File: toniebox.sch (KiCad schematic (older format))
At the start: 129 parts, among them K2 Micro_SD_Card_Det_Hirose_DM3CS, K4 Conn_01x03, K9 Conn_01x03, T11 FDV301N, T360 FDV301N, T4 FDV301N, T5 FDV301N, T6 FDV301N, T7 FDV301N, U1 TLV320DAC3100, U2 CC3200R1M2RGCR, U3 IS25LQ032B-JNLE, U4 MMA8451QT, U8 AP2112K-3.3, U9 AP2120N-1.8

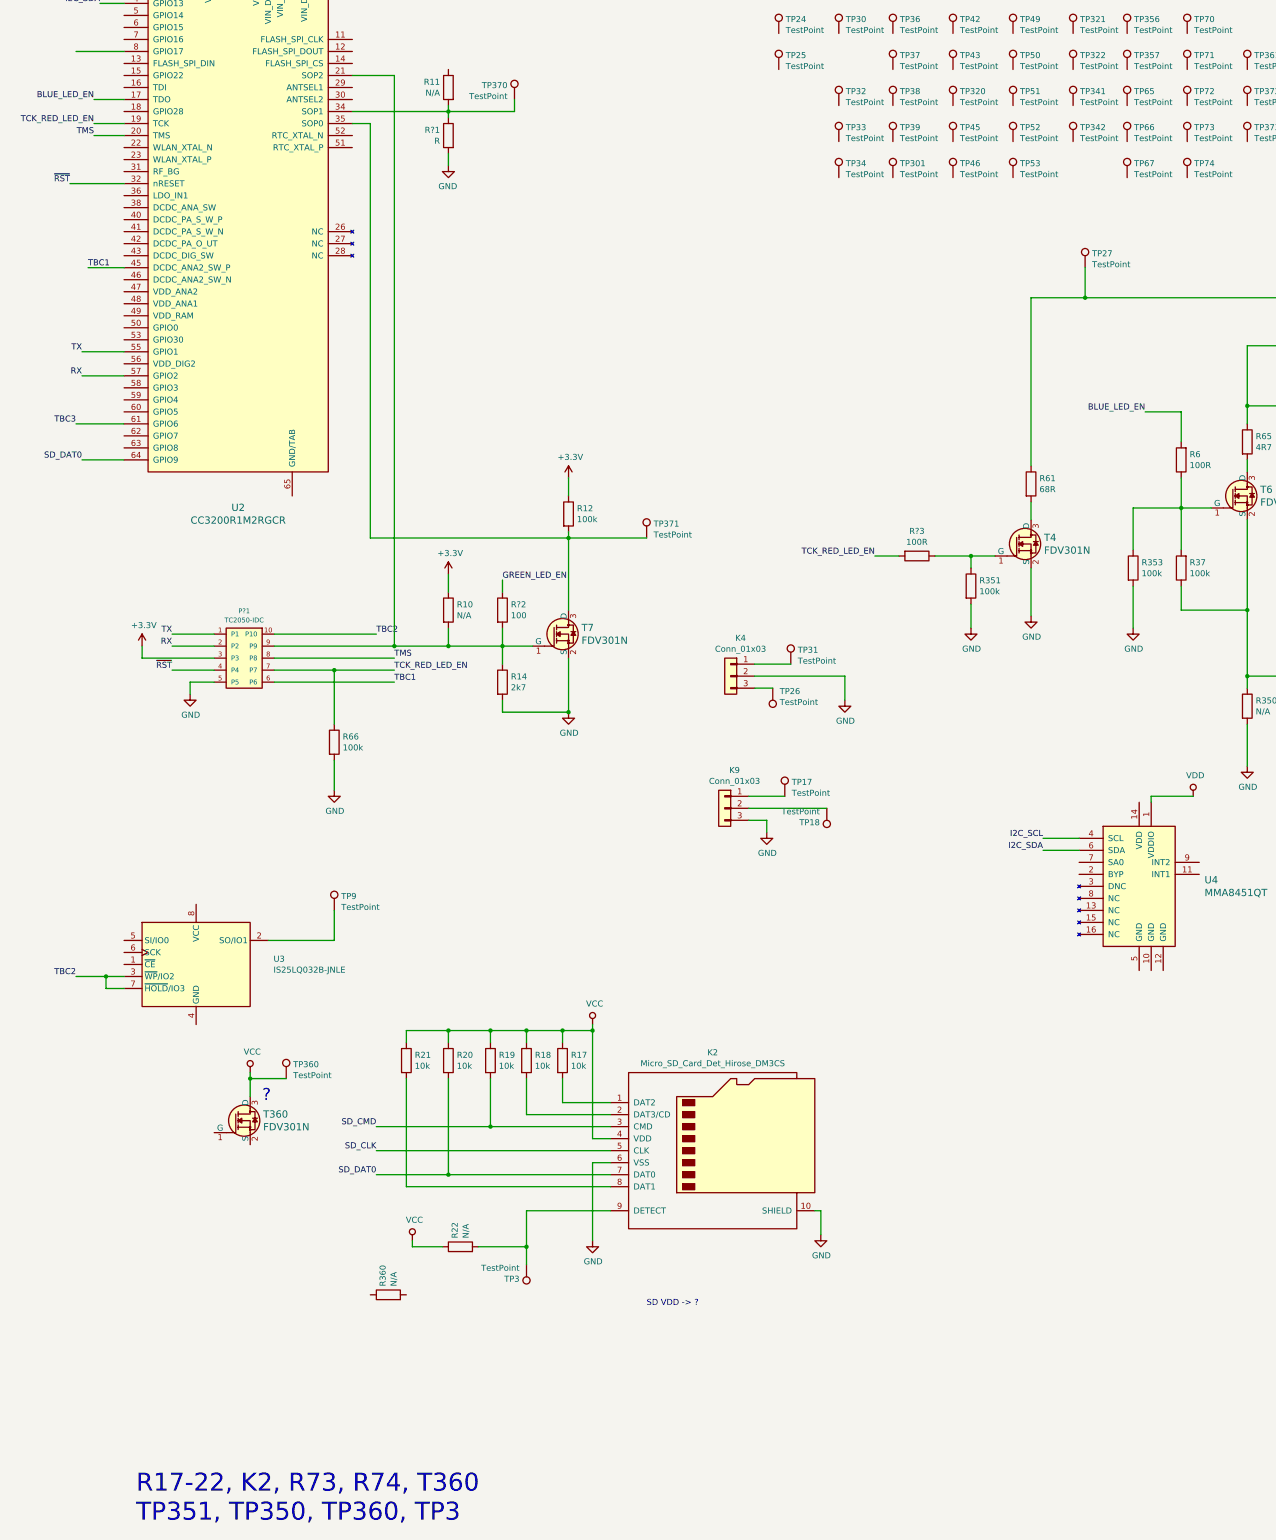
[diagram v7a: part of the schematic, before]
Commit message: battery, ear connectors;datasheets
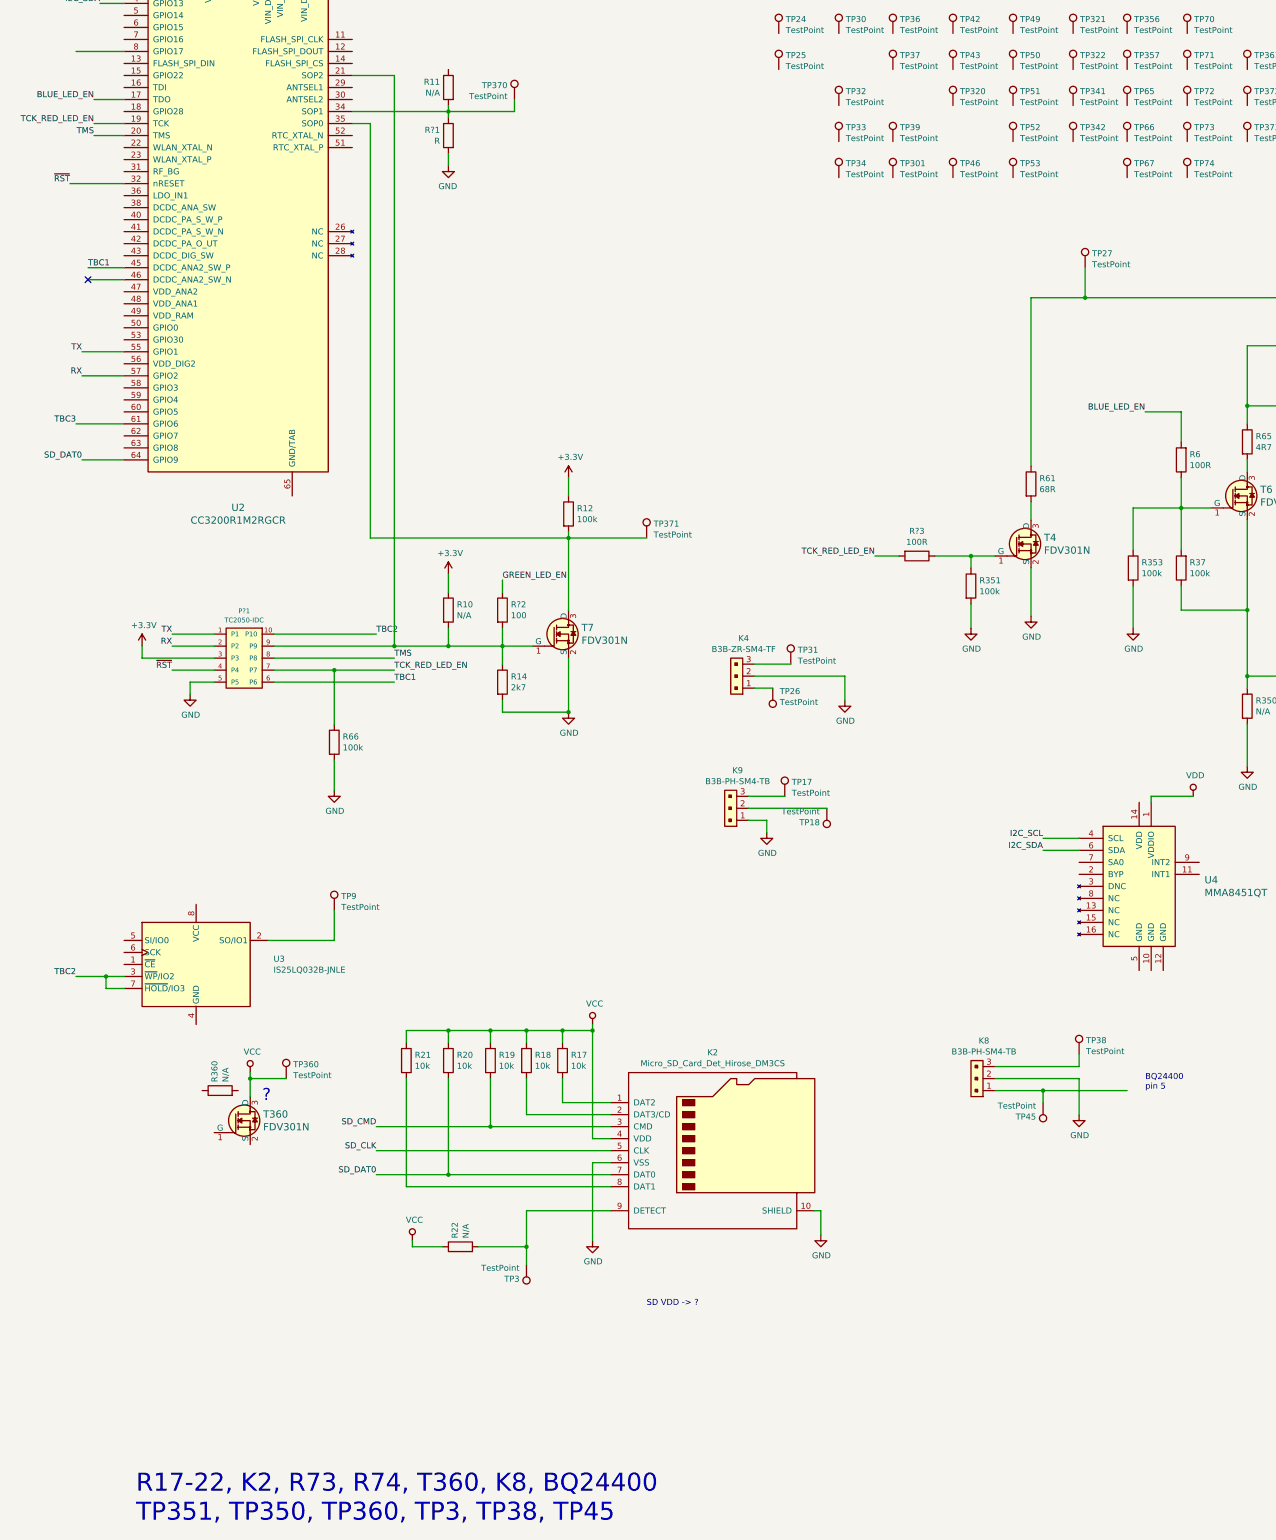
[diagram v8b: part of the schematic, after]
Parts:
- removed K4, K9: Conn_01x03, symbol Connector_Generic:Conn_01x03
- added K4: B3B-ZR-SM4-TF, symbol dk_Rectangular-Connectors-Headers-Male-Pins:B3B-PH-K-S_LF__SN_
- added K8, K9: B3B-PH-SM4-TB, symbol dk_Rectangular-Connectors-Headers-Male-Pins:B3B-PH-K-S_LF__SN_
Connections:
- net GND: now also K4.2, K8.2, K9.1
- net at TP17.1: now also K9.3
- net at TP18.1: now also K9.2
- net at TP31.1: now also K4.3
- net at TP26.1: now also K4.1
- net at TP38.1: now also K8.3
- net at TP45.1: now also K8.1
- no-connect marks 0 -> 1
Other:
- note added: "BQ24400\npin 5\n"
- note added: "R17-22, K2, R73, R74, T360, K8, BQ24400\nTP351, TP350, TP360, TP3, TP38, TP45"
- note removed: "R17-22, K2, R73, R74, T360\nTP351, TP350, TP360, TP3"
- moved on the sheet: R360, TP38, TP45
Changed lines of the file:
@@
 L Connector:TestPoint TP38
 U 1 1 5E31677D
-P 7450 2800
-F 0 "TP38" H 7508 2918 50  0000 L CNN
-F 1 "TestPoint" H 7508 2827 50  0000 L CNN
-F 2 "" H 7650 2800 50  0001 C CNN
-F 3 "~" H 7650 2800 50  0001 C CNN
-	1    7450 2800
+P 9000 10700
+F 0 "TP38" H 9058 10818 50  0000 L CNN
+F 1 "TestPoint" H 9058 10727 50  0000 L CNN
+F 2 "" H 9200 10700 50  0001 C CNN
+F 3 "~" H 9200 10700 50  0001 C CNN
+	1    9000 10700
 	1    0    0    -1
 $EndComp
@@
 L Connector:TestPoint TP45
 U 1 1 5E3167E1
-P 7950 3100
-F 0 "TP45" H 8008 3218 50  0000 L CNN
-F 1 "TestPoint" H 8008 3127 50  0000 L CNN
-F 2 "" H 8150 3100 50  0001 C CNN
-F 3 "~" H 8150 3100 50  0001 C CNN
-	1    7950 3100
-	1    0    0    -1
+P 8700 11100
+F 0 "TP45" H 8758 11218 50  0000 L CNN
+F 1 "TestPoint" H 8758 11127 50  0000 L CNN
+F 2 "" H 8900 11100 50  0001 C CNN
+F 3 "~" H 8900 11100 50  0001 C CNN
+	1    8700 11100
+	-1   0    0    1
 $EndComp
 $Comp
@@
 Wire Wire Line
 	6250 8650 6900 8650
-$Comp
-L Connector_Generic:Conn_01x03 K9
-U 1 1 5E37BC23
-P 6050 8650
-F 0 "K9" H 5968 8967 50  0000 C CNN
-F 1 "Conn_01x03" H 5968 8876 50  0000 C CNN
-F 2 "" H 6050 8650 50  0001 C CNN
-F 3 "~" H 6050 8650 50  0001 C CNN
-	1    6050 8650
-	-1   0    0    -1
-$EndComp
 Wire Wire Line
 	6300 7450 6600 7450
@@
 Wire Wire Line
 	6300 7550 7050 7550
-$Comp
-L Connector_Generic:Conn_01x03 K4
-U 1 1 5E34806A
-P 6100 7550
-F 0 "K4" H 6018 7867 50  0000 C CNN
-F 1 "Conn_01x03" H 6018 7776 50  0000 C CNN
-F 2 "" H 6100 7550 50  0001 C CNN
-F 3 "~" H 6100 7550 50  0001 C CNN
-	1    6100 7550
-	-1   0    0    -1
-$EndComp
 $Comp
 L Connector:TestPoint TP18
@@
 	4400 12450 4400 12300
 Text Notes 1150 14600 0    150  ~ 0
-R17-22, K2, R73, R74, T360\nTP351, TP350, TP360, TP3
+R17-22, K2, R73, R74, T360, K8, BQ24400\nTP351, TP350, TP360, TP3, TP38, TP45
 Text Notes 5400 12800 0    50   ~ 0
 SD VDD -> ?
@@
 L Device:R R360
 U 1 1 5E72EE90
-P 3250 12700
-F 0 "R360" H 3320 12746 50  0000 L CNN
-F 1 "N/A" H 3320 12655 50  0000 L CNN
-F 2 "" V 3180 12700 50  0001 C CNN
-F 3 "~" H 3250 12700 50  0001 C CNN
-	1    3250 12700
+P 1850 11000
+F 0 "R360" H 1920 11046 50  0000 L CNN
+F 1 "N/A" H 1920 10955 50  0000 L CNN
+F 2 "" V 1780 11000 50  0001 C CNN
+F 3 "~" H 1850 11000 50  0001 C CNN
+	1    1850 11000
 	0    -1   -1   0
 $EndComp
@@
 Wire Wire Line
 	4100 11300 5100 11300
+Wire Wire Line
+	1050 4250 750  4250
+NoConn ~ 750  4250
+$Comp
+L dk_Rectangular-Connectors-Headers-Male-Pins:B3B-PH-K-S_LF__SN_ K9
+U 1 1 5E555946
+P 6100 8750
+F 0 "K9" V 6515 8808 50  0000 C CNN
+F 1 "B3B-PH-SM4-TB" V 6424 8808 50  0000 C CNN
+F 2 "" H 6300 8950 60  0001 L CNN
+F 3 "http://www.jst-mfg.com/product/pdf/eng/ePH.pdf" H 6300 9050 60  0001 L CNN
+F 4 "455-1735-1-ND" H 6300 9150 60  0001 L CNN "Digi-Key_PN"
+F 5 "B3B-PH-SM4-TB(LF)(SN)" H 6300 9250 60  0001 L CNN "MPN"
+F 6 "Connectors, Interconnects" H 6300 9350 60  0001 L CNN "Category"
+F 7 "Rectangular Connectors - Headers, Male Pins" H 6300 9450 60  0001 L CNN "Family"
+F 8 "http://www.jst-mfg.com/product/pdf/eng/ePH.pdf" H 6300 9550 60  0001 L CNN "DK_Datasheet_Link"
+F 9 "" H 6300 9650 60  0001 L CNN "DK_Detail_Page"
+F 10 "CONN HEADER VERT 3POS 2MM" H 6300 9750 60  0001 L CNN "Description"
+F 11 "JST Sales America Inc." H 6300 9850 60  0001 L CNN "Manufacturer"
+F 12 "Active" H 6300 9950 60  0001 L CNN "Status"
+	1    6100 8750
+	0    1    -1   0
+$EndComp
+$Comp
+L dk_Rectangular-Connectors-Headers-Male-Pins:B3B-PH-K-S_LF__SN_ K8
+U 1 1 5E5571CA
+P 8150 11000
+F 0 "K8" V 8565 11058 50  0000 C CNN
+F 1 "B3B-PH-SM4-TB" V 8474 11058 50  0000 C CNN
+F 2 "" H 8350 11200 60  0001 L CNN
+F 3 "http://www.jst-mfg.com/product/pdf/eng/ePH.pdf" H 8350 11300 60  0001 L CNN
+F 4 "455-1735-1-ND" H 8350 11400 60  0001 L CNN "Digi-Key_PN"
+F 5 "B3B-PH-SM4-TB(LF)(SN)" H 8350 11500 60  0001 L CNN "MPN"
+F 6 "Connectors, Interconnects" H 8350 11600 60  0001 L CNN "Category"
+F 7 "Rectangular Connectors - Headers, Male Pins" H 8350 11700 60  0001 L CNN "Family"
+F 8 "http://www.jst-mfg.com/product/pdf/eng/ePH.pdf" H 8350 11800 60  0001 L CNN "DK_Datasheet_Link"
+F 9 "" H 8350 11900 60  0001 L CNN "DK_Detail_Page"
+F 10 "CONN HEADER VERT 3POS 2MM" H 8350 12000 60  0001 L CNN "Description"
+F 11 "JST Sales America Inc." H 8350 12100 60  0001 L CNN "Manufacturer"
+F 12 "Active" H 8350 12200 60  0001 L CNN "Status"
+	1    8150 11000
+	0    1    -1   0
+$EndComp
+Wire Wire Line
+	8300 10900 9000 10900
+Wire Wire Line
+	9000 10900 9000 11200
+$Comp
+L power:GND #PWR?
+U 1 1 5E565A7A
+P 9000 11200
+F 0 "#PWR?" H 9000 10950 50  0001 C CNN
+F 1 "GND" H 9005 11027 50  0000 C CNN
+F 2 "" H 9000 11200 50  0001 C CNN
+F 3 "" H 9000 11200 50  0001 C CNN
+	1    9000 11200
+	1    0    0    -1
+$EndComp
+Wire Wire Line
+	8300 10800 9000 10800
+Wire Wire Line
+	9000 10800 9000 10700
+Wire Wire Line
+	8300 11000 8700 11000
+Wire Wire Line
+	8700 11000 8700 11100
+Wire Wire Line
+	8700 11000 9400 11000
+Connection ~ 8700 11000
+Text Notes 9550 11000 0    50   ~ 0
+BQ24400\npin 5\n
+$Comp
+L dk_Rectangular-Connectors-Headers-Male-Pins:B3B-PH-K-S_LF__SN_ K4
+U 1 1 5E59A21A
+P 6150 7650
+F 0 "K4" V 6565 7708 50  0000 C CNN
+F 1 "B3B-ZR-SM4-TF" V 6474 7708 50  0000 C CNN
+F 2 "" H 6350 7850 60  0001 L CNN
+F 3 "http://www.jst-mfg.com/product/pdf/eng/eZH.pdf" H 6350 7950 60  0001 L CNN
+F 4 "455-1682-1-ND" H 6350 8050 60  0001 L CNN "Digi-Key_PN"
+F 5 "B3B-ZR-SM4-TF(LF)(SN)" H 6350 8150 60  0001 L CNN "MPN"
+F 6 "Connectors, Interconnects" H 6350 8250 60  0001 L CNN "Category"
+F 7 "Rectangular Connectors - Headers, Male Pins" H 6350 8350 60  0001 L CNN "Family"
+F 8 "http://www.jst-mfg.com/product/pdf/eng/eZH.pdf" H 6350 8450 60  0001 L CNN "DK_Datasheet_Link"
+F 9 "" H 6350 8550 60  0001 L CNN "DK_Detail_Page"
+F 10 "CONN HEADER VERT 3POS 1.5MM" H 6350 8650 60  0001 L CNN "Description"
+F 11 "JST Sales America Inc." H 6350 8750 60  0001 L CNN "Manufacturer"
+F 12 "Active" H 6350 8850 60  0001 L CNN "Status"
+	1    6150 7650
+	0    1    -1   0
+$EndComp
 $EndSCHEMATC
